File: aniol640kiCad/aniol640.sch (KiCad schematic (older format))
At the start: 41 parts, among them J1 RST, J2 PWR, U12 74LS74, U2 74LS14, U4 74LS32, U5 74LS08, X1 ACO-1.8432MHz

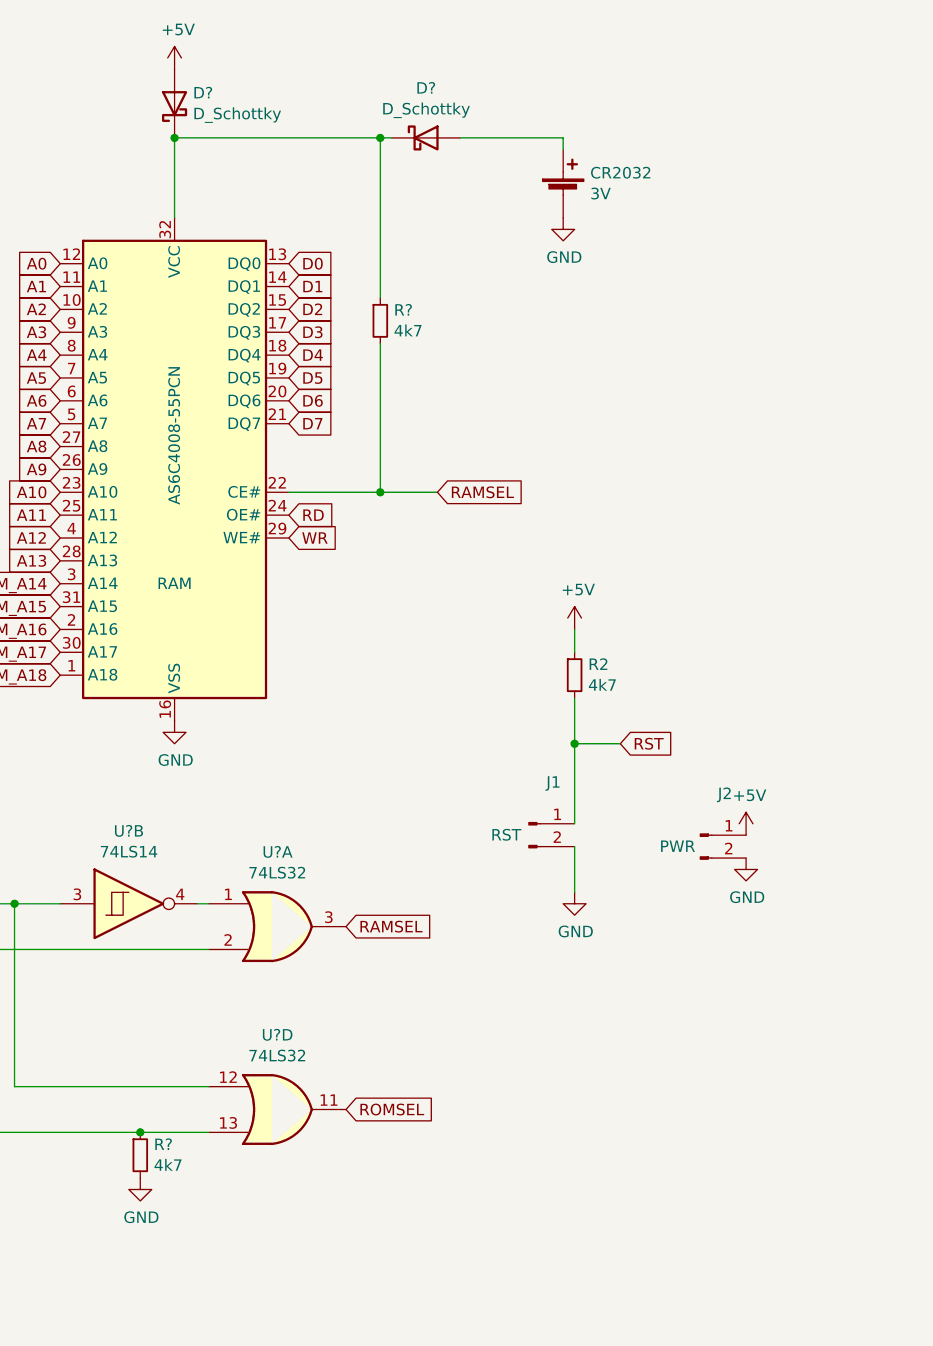
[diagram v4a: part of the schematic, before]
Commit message: Updated the schematic
- added inverted DART clock
- added power-up reset
- changed to the more simplified ROM address decoding
- removed battery backup for RAM
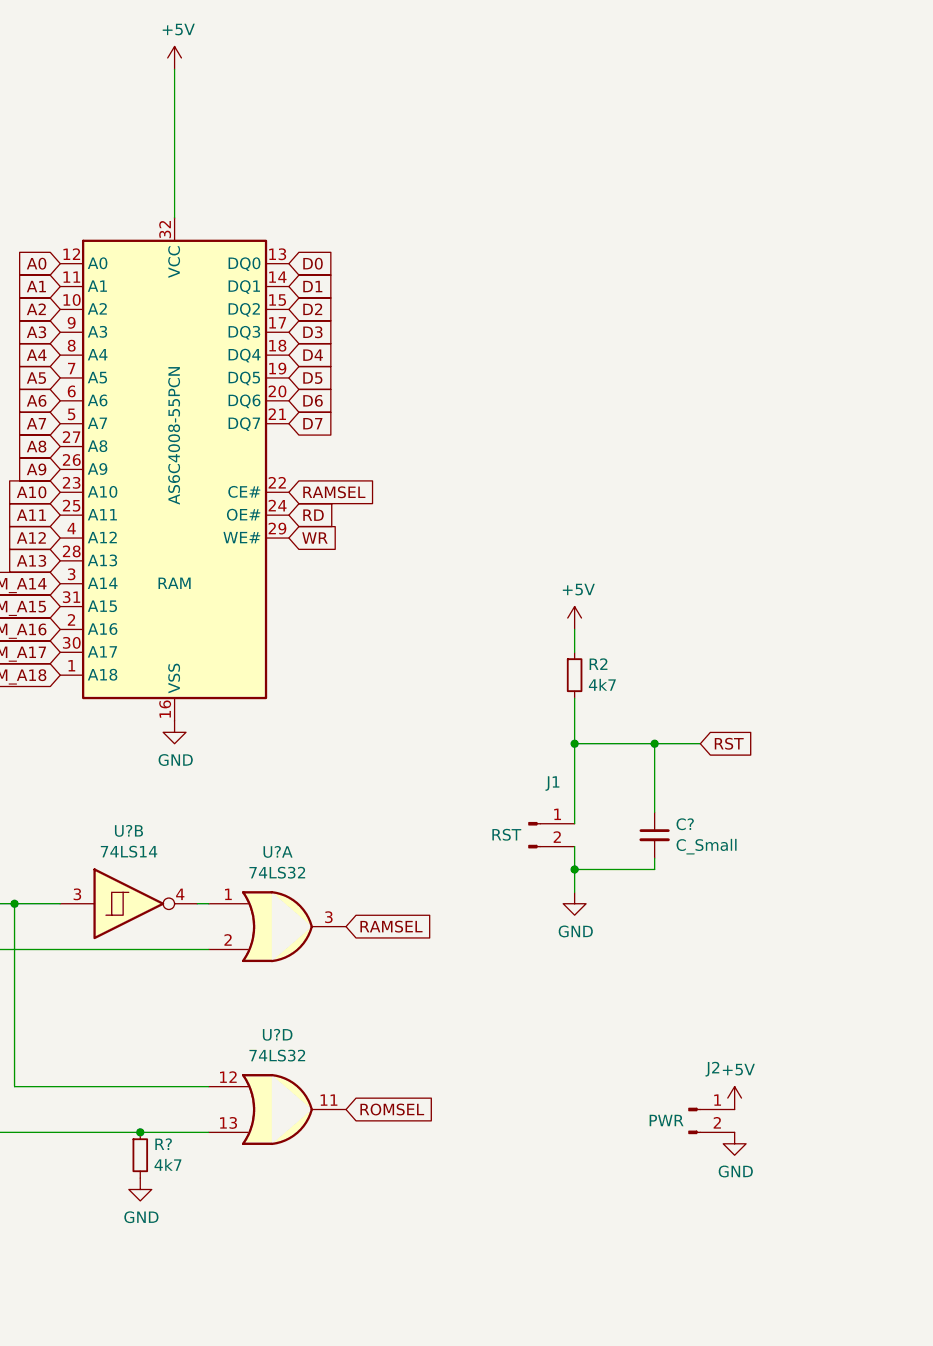
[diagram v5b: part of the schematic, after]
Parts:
- removed CR2032: 3V, symbol Device:Battery_Cell
- removed D? (x2): D_Schottky, symbol Device:D_Schottky
- removed R?: 4k7, symbol Device:R_Small
- added C?: C_Small, symbol Device:C_Small
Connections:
- net +5V: now also RAM.32 (VCC)
- net GND: now also C?.2
- net RST: now also C?.1
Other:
- moved on the sheet: J2
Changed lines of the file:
@@
 Wire Wire Line
 	10200 3850 10200 4050
-Text GLabel 10400 4050 2    50   Input ~ 0
+Text GLabel 10750 4050 2    50   Input ~ 0
 RST
-Wire Wire Line
-	10400 4050 10200 4050
 Connection ~ 10200 4050
 $Comp
@@
 L Connector:Conn_01x02_Male J2
 U 1 1 61D552DF
-P 10750 4450
-F 0 "J2" H 10858 4631 50  0000 C CNN
-F 1 "PWR" H 10650 4400 50  0000 C CNN
-F 2 "Connector_PinHeader_2.54mm:PinHeader_1x02_P2.54mm_Vertical" H 10750 4450 50  0001 C CNN
-F 3 "~" H 10750 4450 50  0001 C CNN
-	1    10750 4450
+P 10700 5650
+F 0 "J2" H 10808 5831 50  0000 C CNN
+F 1 "PWR" H 10600 5600 50  0000 C CNN
+F 2 "Connector_PinHeader_2.54mm:PinHeader_1x02_P2.54mm_Vertical" H 10700 5650 50  0001 C CNN
+F 3 "~" H 10700 5650 50  0001 C CNN
+	1    10700 5650
 	1    0    0    -1
 $EndComp
@@
 L power:GND #PWR06
 U 1 1 61D56634
-P 10950 4550
-F 0 "#PWR06" H 10950 4300 50  0001 C CNN
-F 1 "GND" H 10955 4377 50  0000 C CNN
-F 2 "" H 10950 4550 50  0001 C CNN
-F 3 "" H 10950 4550 50  0001 C CNN
-	1    10950 4550
+P 10900 5750
+F 0 "#PWR06" H 10900 5500 50  0001 C CNN
+F 1 "GND" H 10905 5577 50  0000 C CNN
+F 2 "" H 10900 5750 50  0001 C CNN
+F 3 "" H 10900 5750 50  0001 C CNN
+	1    10900 5750
 	1    0    0    -1
 $EndComp
@@
 L power:+5V #PWR05
 U 1 1 61D56F4A
-P 10950 4450
-F 0 "#PWR05" H 10950 4300 50  0001 C CNN
-F 1 "+5V" H 10965 4623 50  0000 C CNN
-F 2 "" H 10950 4450 50  0001 C CNN
-F 3 "" H 10950 4450 50  0001 C CNN
-	1    10950 4450
+P 10900 5650
+F 0 "#PWR05" H 10900 5500 50  0001 C CNN
+F 1 "+5V" H 10915 5823 50  0000 C CNN
+F 2 "" H 10900 5650 50  0001 C CNN
+F 3 "" H 10900 5650 50  0001 C CNN
+	1    10900 5650
 	1    0    0    -1
 $EndComp
@@
 	10200 4050 10200 4400
 Wire Wire Line
-	10200 4500 10200 4700
+	10200 4500 10200 4600
 Wire Wire Line
 	2150 2200 2150 2800
@@
 Text GLabel 6100 3550 0    50   Input ~ 0
 ROMSEL
-Text GLabel 9600 2950 2    50   Input ~ 0
+Text GLabel 8950 2950 2    50   Input ~ 0
 RAMSEL
 Text GLabel 7950 1950 0    50   Input ~ 0
@@
 Wire Wire Line
 	4300 6050 4650 6050
-$Comp
-L Device:D_Schottky D?
-U 1 1 625B1E53
-P 8450 1250
-F 0 "D?" V 8496 1170 50  0000 R CNN
-F 1 "D_Schottky" V 8405 1170 50  0000 R CNN
-F 2 "" H 8450 1250 50  0001 C CNN
-F 3 "~" H 8450 1250 50  0001 C CNN
-	1    8450 1250
-	0    -1   -1   0
-$EndComp
-$Comp
-L Device:D_Schottky D?
-U 1 1 625B23EB
-P 9550 1400
-F 0 "D?" H 9550 1617 50  0000 C CNN
-F 1 "D_Schottky" H 9550 1526 50  0000 C CNN
-F 2 "" H 9550 1400 50  0001 C CNN
-F 3 "~" H 9550 1400 50  0001 C CNN
-	1    9550 1400
-	1    0    0    -1
-$EndComp
-Wire Wire Line
-	8450 1400 8450 1750
-Connection ~ 8450 1400
-Wire Wire Line
-	8450 1400 9350 1400
-$Comp
-L Device:R_Small R?
-U 1 1 625D62BC
-P 9350 2200
-F 0 "R?" H 9409 2246 50  0000 L CNN
-F 1 "4k7" H 9409 2155 50  0000 L CNN
-F 2 "" H 9350 2200 50  0001 C CNN
-F 3 "~" H 9350 2200 50  0001 C CNN
-	1    9350 2200
-	1    0    0    -1
-$EndComp
-Wire Wire Line
-	9350 1400 9350 2100
-Connection ~ 9350 1400
-Wire Wire Line
-	9350 1400 9400 1400
-Wire Wire Line
-	9350 2300 9350 2950
-Wire Wire Line
-	9350 2950 8950 2950
-Wire Wire Line
-	9350 2950 9600 2950
-Connection ~ 9350 2950
-$Comp
-L Device:Battery_Cell CR2032
-U 1 1 625E844B
-P 10150 1650
-F 0 "CR2032" H 10268 1746 50  0000 L CNN
-F 1 "3V" H 10268 1655 50  0000 L CNN
-F 2 "" V 10150 1710 50  0001 C CNN
-F 3 "~" V 10150 1710 50  0001 C CNN
-	1    10150 1650
-	1    0    0    -1
-$EndComp
-Wire Wire Line
-	10150 1450 10150 1400
-Wire Wire Line
-	10150 1400 9700 1400
-$Comp
-L power:GND #PWR?
-U 1 1 625F0565
-P 10150 1750
-F 0 "#PWR?" H 10150 1500 50  0001 C CNN
-F 1 "GND" H 10155 1577 50  0000 C CNN
-F 2 "" H 10150 1750 50  0001 C CNN
-F 3 "" H 10150 1750 50  0001 C CNN
-	1    10150 1750
-	1    0    0    -1
-$EndComp
 Wire Wire Line
 	8600 5750 8300 5750
@@
 Wire Wire Line
 	7750 4750 7750 5550
+Wire Wire Line
+	8450 1100 8450 1750
+Wire Wire Line
+	10200 4050 10550 4050
+$Comp
+L Device:C_Small C?
+U 1 1 63257D20
+P 10550 4450
+F 0 "C?" H 10642 4496 50  0000 L CNN
+F 1 "C_Small" H 10642 4405 50  0000 L CNN
+F 2 "" H 10550 4450 50  0001 C CNN
+F 3 "~" H 10550 4450 50  0001 C CNN
+	1    10550 4450
+	1    0    0    -1
+$EndComp
+Wire Wire Line
+	10550 4350 10550 4050
+Connection ~ 10550 4050
+Wire Wire Line
+	10550 4050 10750 4050
+Wire Wire Line
+	10550 4550 10550 4600
+Wire Wire Line
+	10550 4600 10200 4600
+Connection ~ 10200 4600
+Wire Wire Line
+	10200 4600 10200 4700
 $EndSCHEMATC

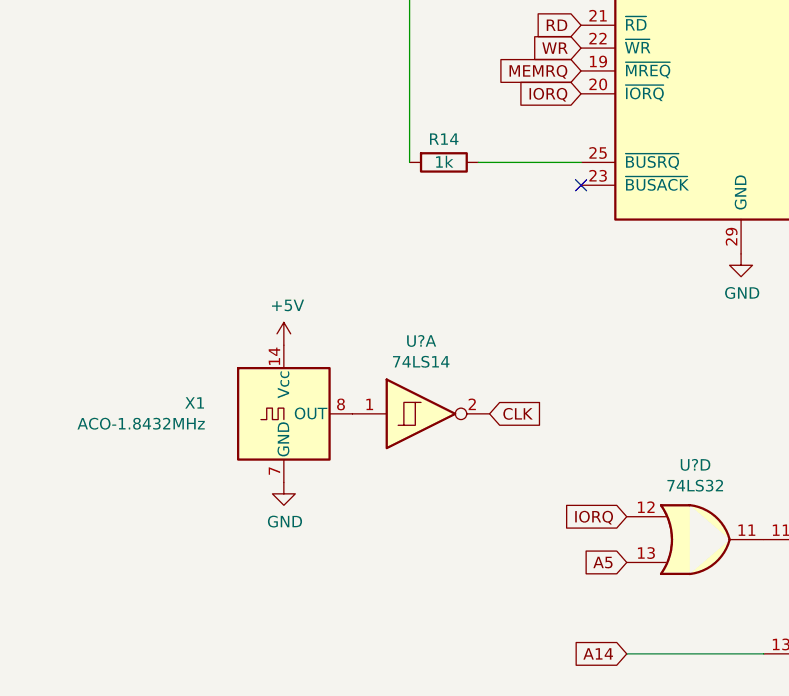
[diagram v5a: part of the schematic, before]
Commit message: 8088 project added
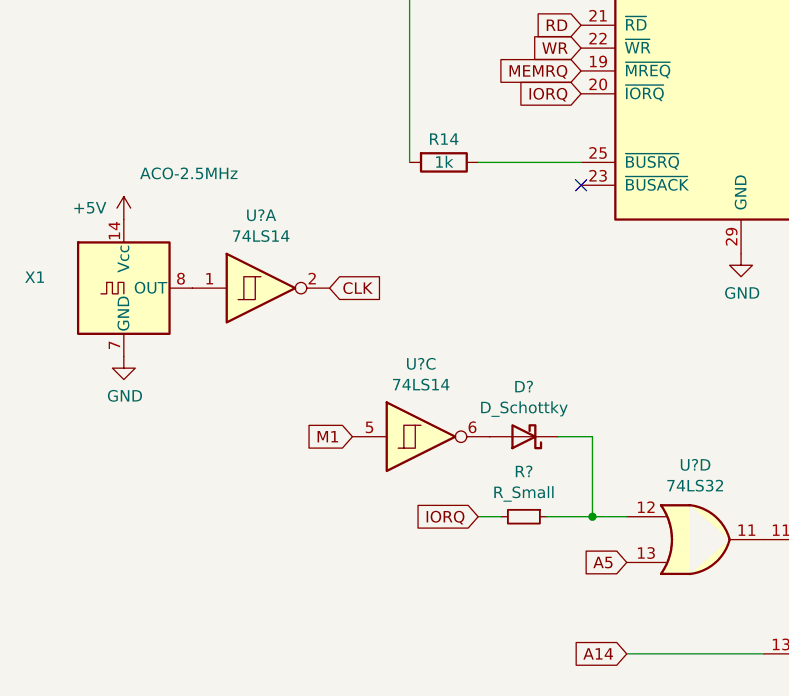
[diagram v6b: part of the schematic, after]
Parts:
- added D?: D_Schottky, symbol Device:D_Schottky
- added R?: R_Small, symbol Device:R_Small
- added U?: 74LS14, symbol 74xx:74LS14
- X1: value ACO-1.8432MHz -> ACO-2.5MHz
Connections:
- net IORQ: now also R?.2; no longer U?.12
- net M1: now also U?.5
- new net: D?.1 (K), R?.1, U?.12
- new net: D?.2 (A), U?.6
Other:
- moved on the sheet: U?A, X1
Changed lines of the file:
@@
 L Oscillator:ACO-xxxMHz X1
 U 1 1 61D3D043
-P 1600 5000
-F 0 "X1" H 1257 5046 50  0000 R CNN
-F 1 "ACO-1.8432MHz" H 1257 4955 50  0000 R CNN
-F 2 "Oscillator:Oscillator_DIP-14" H 2050 4650 50  0001 C CNN
-F 3 "http://www.conwin.com/datasheets/cx/cx030.pdf" H 1500 5000 50  0001 C CNN
-	1    1600 5000
+P 900 4450
+F 0 "X1" H 557 4496 50  0000 R CNN
+F 1 "ACO-2.5MHz" H 1400 4950 50  0000 R CNN
+F 2 "Oscillator:Oscillator_DIP-14" H 1350 4100 50  0001 C CNN
+F 3 "http://www.conwin.com/datasheets/cx/cx030.pdf" H 800 4450 50  0001 C CNN
+	1    900  4450
 	1    0    0    -1
 $EndComp
@@
 L power:+5V #PWR014
 U 1 1 61D3E347
-P 1600 4700
-F 0 "#PWR014" H 1600 4550 50  0001 C CNN
-F 1 "+5V" H 1615 4873 50  0000 C CNN
-F 2 "" H 1600 4700 50  0001 C CNN
-F 3 "" H 1600 4700 50  0001 C CNN
-	1    1600 4700
+P 900 4150
+F 0 "#PWR014" H 900 4000 50  0001 C CNN
+F 1 "+5V" H 750 4200 50  0000 C CNN
+F 2 "" H 900 4150 50  0001 C CNN
+F 3 "" H 900 4150 50  0001 C CNN
+	1    900  4150
 	1    0    0    -1
 $EndComp
@@
 L power:GND #PWR015
 U 1 1 61D3EB67
-P 1600 5300
-F 0 "#PWR015" H 1600 5050 50  0001 C CNN
-F 1 "GND" H 1605 5127 50  0000 C CNN
-F 2 "" H 1600 5300 50  0001 C CNN
-F 3 "" H 1600 5300 50  0001 C CNN
-	1    1600 5300
+P 900 4750
+F 0 "#PWR015" H 900 4500 50  0001 C CNN
+F 1 "GND" H 905 4577 50  0000 C CNN
+F 2 "" H 900 4750 50  0001 C CNN
+F 3 "" H 900 4750 50  0001 C CNN
+	1    900  4750
 	1    0    0    -1
 $EndComp
@@
 L 74xx:74LS14 U?
 U 1 1 62490009
-P 2200 5000
-F 0 "U?" H 2200 5317 50  0000 C CNN
-F 1 "74LS14" H 2200 5226 50  0000 C CNN
-F 2 "" H 2200 5000 50  0001 C CNN
-F 3 "http://www.ti.com/lit/gpn/sn74LS14" H 2200 5000 50  0001 C CNN
-	1    2200 5000
-	1    0    0    -1
-$EndComp
-Text GLabel 2500 5000 2    50   Input ~ 0
+P 1500 4450
+F 0 "U?" H 1500 4767 50  0000 C CNN
+F 1 "74LS14" H 1500 4676 50  0000 C CNN
+F 2 "" H 1500 4450 50  0001 C CNN
+F 3 "http://www.ti.com/lit/gpn/sn74LS14" H 1500 4450 50  0001 C CNN
+	1    1500 4450
+	1    0    0    -1
+$EndComp
+Text GLabel 1800 4450 2    50   Input ~ 0
 CLK
 $Comp
@@
 Text GLabel 3100 5650 0    50   Input ~ 0
 A5
-Text GLabel 3100 5450 0    50   Input ~ 0
+Text GLabel 2450 5450 0    50   Input ~ 0
 IORQ
 $Comp
@@
 Wire Wire Line
 	10200 4600 10200 4700
+$Comp
+L Device:R_Small R?
+U 1 1 63343F4D
+P 2650 5450
+F 0 "R?" V 2454 5450 50  0000 C CNN
+F 1 "R_Small" V 2545 5450 50  0000 C CNN
+F 2 "" H 2650 5450 50  0001 C CNN
+F 3 "~" H 2650 5450 50  0001 C CNN
+	1    2650 5450
+	0    1    1    0
+$EndComp
+Wire Wire Line
+	2550 5450 2450 5450
+Wire Wire Line
+	3100 5450 2950 5450
+$Comp
+L Device:D_Schottky D?
+U 1 1 6335B52C
+P 2650 5100
+F 0 "D?" H 2650 4883 50  0000 C CNN
+F 1 "D_Schottky" H 2650 4974 50  0000 C CNN
+F 2 "" H 2650 5100 50  0001 C CNN
+F 3 "~" H 2650 5100 50  0001 C CNN
+	1    2650 5100
+	-1   0    0    1
+$EndComp
+Wire Wire Line
+	2800 5100 2950 5100
+Wire Wire Line
+	2950 5100 2950 5450
+Connection ~ 2950 5450
+Wire Wire Line
+	2950 5450 2750 5450
+$Comp
+L 74xx:74LS14 U?
+U 3 1 63362105
+P 2200 5100
+F 0 "U?" H 2200 5417 50  0000 C CNN
+F 1 "74LS14" H 2200 5326 50  0000 C CNN
+F 2 "" H 2200 5100 50  0001 C CNN
+F 3 "http://www.ti.com/lit/gpn/sn74LS14" H 2200 5100 50  0001 C CNN
+	3    2200 5100
+	1    0    0    -1
+$EndComp
+Text GLabel 1900 5100 0    50   Input ~ 0
+M1
 $EndSCHEMATC
